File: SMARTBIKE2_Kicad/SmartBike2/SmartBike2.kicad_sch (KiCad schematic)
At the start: 0 parts

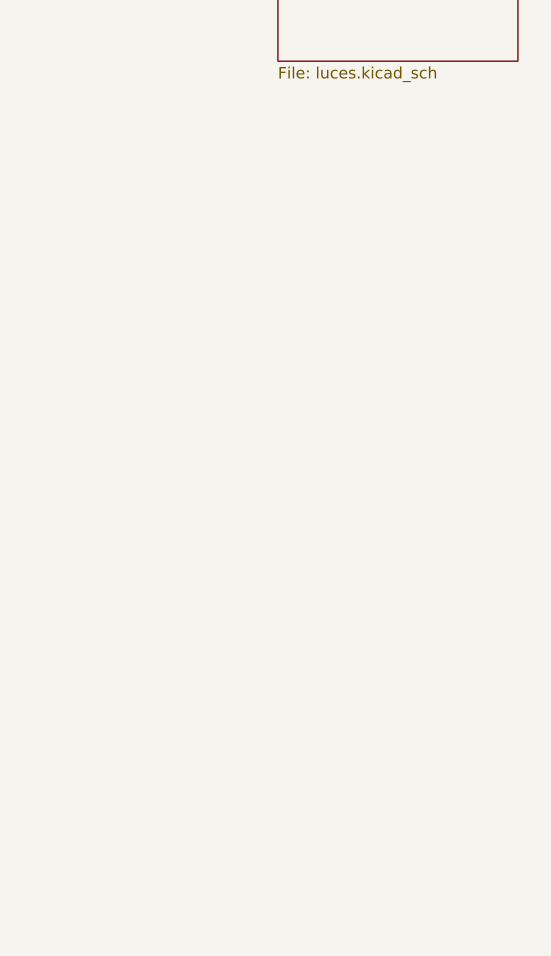
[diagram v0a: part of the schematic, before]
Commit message: Alarma, luces frontales y modulos
+ Circuito luces frontales
+ Conector Luces
+ Conector GPS
+ Conector SIM
+ Conector acelerómetro

~ Acondicionamiento ESP32
~ Huellas
~ PCB
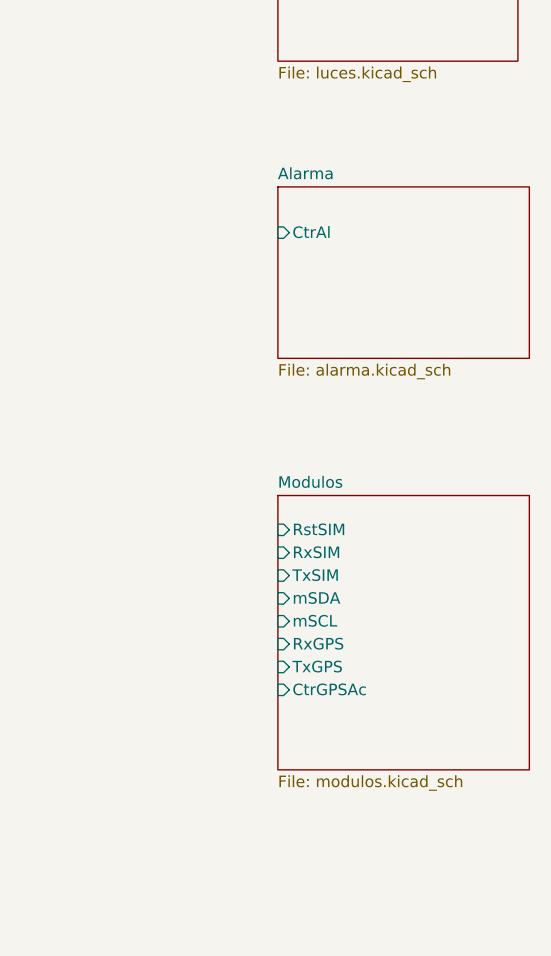
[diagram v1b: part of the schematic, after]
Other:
- added sheet Alarma (alarma.kicad_sch)
- added sheet Modulos (modulos.kicad_sch)
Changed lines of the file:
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@@
 (kicad_sch (version 20230121) (generator eeschema)
   (paper "A4")
+  (sheet (at 232.41 71.12) (size 27.94 19.05) (fields_autoplaced)
+    (stroke (width 0.1524) (type solid))
+    (fill (color 0 0 0 0.0000))
+    (property "Sheetname" "Alarma" (at 232.41 70.4084 0)
+      (effects (font (size 1.27 1.27)) (justify left bottom))
+    )
+    (property "Sheetfile" "alarma.kicad_sch" (at 232.41 90.7546 0)
+      (effects (font (size 1.27 1.27)) (justify left top))
+    )
+    (pin "CtrAl" input (at 232.41 76.2 180)
+      (effects (font (size 1.27 1.27)) (justify left))
+    )
+    (instances
+      (project "SmartBike2"
+        (path "/ec60d9f0-678c-40dc-aaf4-e99b29a92238" (page "6"))
+      )
+    )
+  )
   (sheet (at 232.41 35.56) (size 26.67 21.59) (fields_autoplaced)
     (stroke (width 0.1524) (type solid))
@@
       )
     )
+  )
+  (sheet (at 232.41 105.41) (size 27.94 30.48) (fields_autoplaced)
+    (stroke (width 0.1524) (type solid))
+    (fill (color 0 0 0 0.0000))
+    (property "Sheetname" "Modulos" (at 232.41 104.6984 0)
+      (effects (font (size 1.27 1.27)) (justify left bottom))
+    )
+    (property "Sheetfile" "modulos.kicad_sch" (at 232.41 136.4746 0)
+      (effects (font (size 1.27 1.27)) (justify left top))
+    )
+    (pin "RstSIM" input (at 232.41 109.22 180)
+      (effects (font (size 1.27 1.27)) (justify left))
+    )
+    (pin "RxSIM" input (at 232.41 111.76 180)
+      (effects (font (size 1.27 1.27)) (justify left))
+    )
+    (pin "TxSIM" input (at 232.41 114.3 180)
+      (effects (font (size 1.27 1.27)) (justify left))
+    )
+    (pin "mSDA" input (at 232.41 116.84 180)
+      (effects (font (size 1.27 1.27)) (justify left))
+    )
+    (pin "mSCL" input (at 232.41 119.38 180)
+      (effects (font (size 1.27 1.27)) (justify left))
+    )
+    (pin "RxGPS" input (at 232.41 121.92 180)
+      (effects (font (size 1.27 1.27)) (justify left))
+    )
+    (pin "TxGPS" input (at 232.41 124.46 180)
+      (effects (font (size 1.27 1.27)) (justify left))
+    )
+    (pin "CtrGPSAc" input (at 232.41 127 180)
+      (effects (font (size 1.27 1.27)) (justify left))
+    )
+    (instances
+      (project "SmartBike2"
+        (path "/ec60d9f0-678c-40dc-aaf4-e99b29a92238" (page "7"))
+      )
+    )

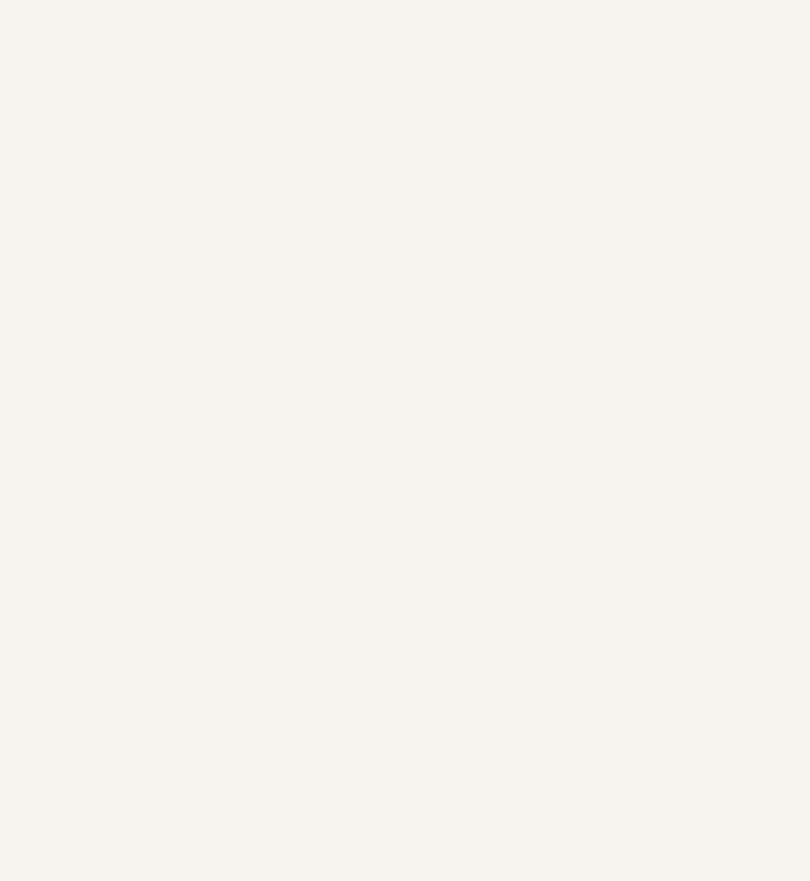
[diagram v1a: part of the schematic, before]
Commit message: Simbolo ESP32
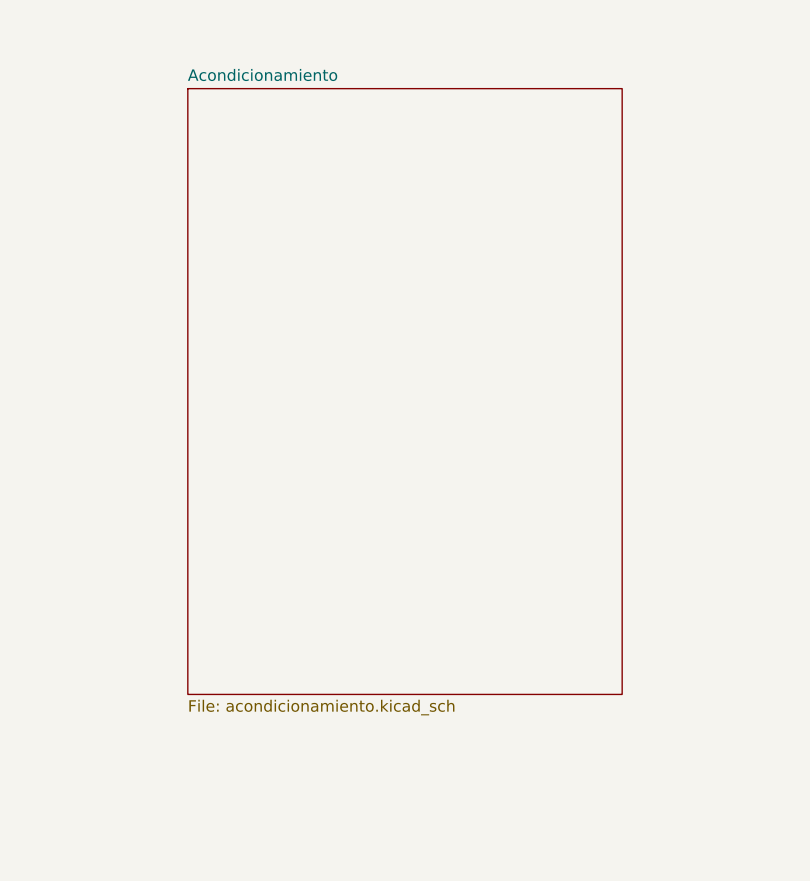
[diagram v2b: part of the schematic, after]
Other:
- added sheet Acondicionamiento (acondicionamiento.kicad_sch)
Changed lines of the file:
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@@
+    )
+  )
+  (sheet (at 58.42 40.64) (size 48.26 67.31) (fields_autoplaced)
+    (stroke (width 0.1524) (type solid))
+    (fill (color 0 0 0 0.0000))
+    (property "Sheetname" "Acondicionamiento" (at 58.42 39.9284 0)
+      (effects (font (size 1.27 1.27)) (justify left bottom))
+    )
+    (property "Sheetfile" "acondicionamiento.kicad_sch" (at 58.42 108.5346 0)
+      (effects (font (size 1.27 1.27)) (justify left top))
+    )
+    (instances
+      (project "SmartBike2"
+        (path "/ec60d9f0-678c-40dc-aaf4-e99b29a92238" (page "8"))
+      )
     )
   )

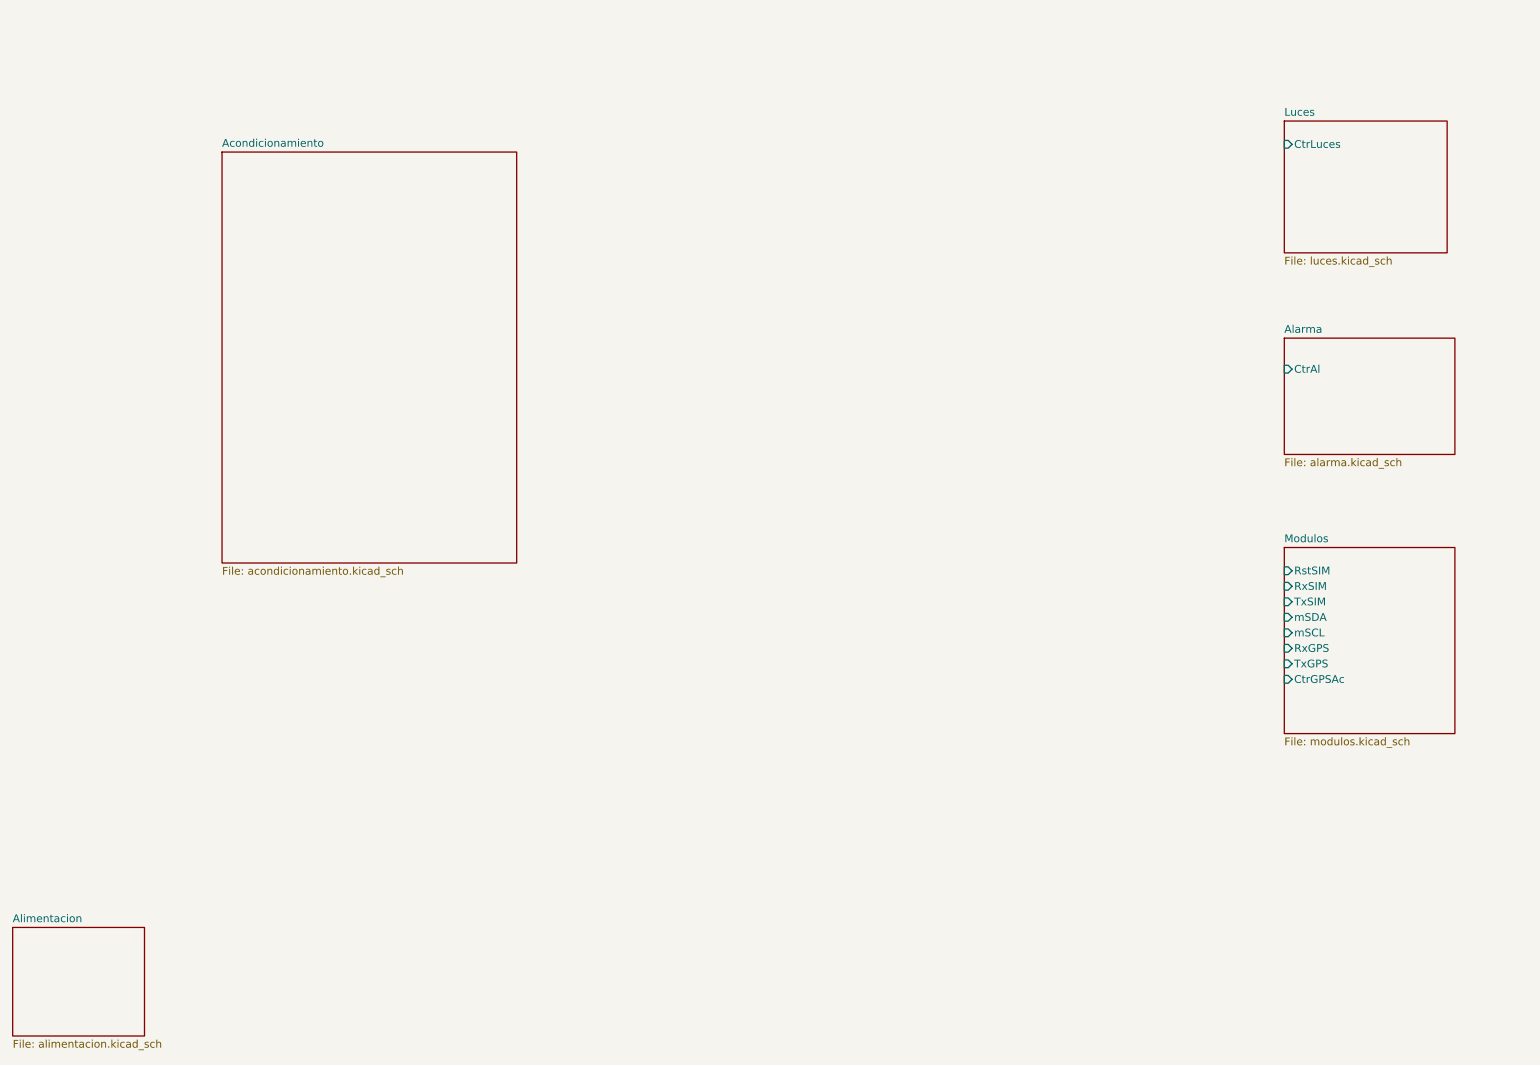
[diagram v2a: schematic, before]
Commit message: Beta 100% esquemáticos
+ Acondicionamiento ESP32

~ Huellas
~ PCB
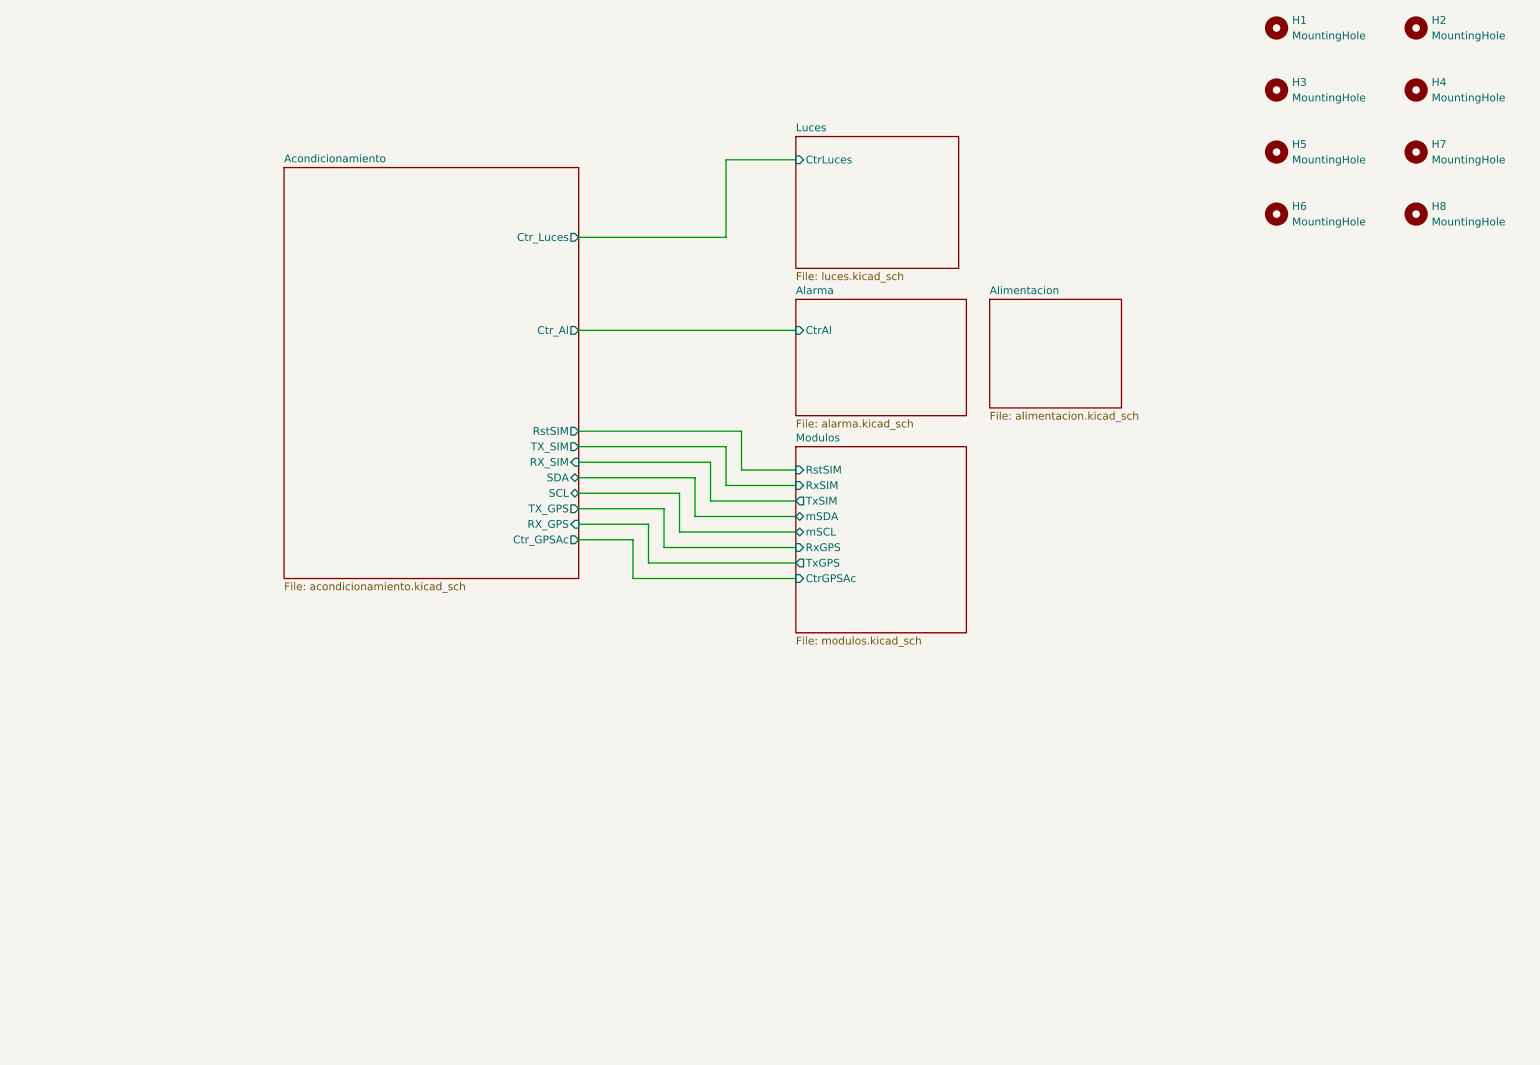
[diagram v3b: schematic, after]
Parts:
- added H1, H2, H3, H4, H5, H6, H7, H8: MountingHole, symbol Mechanical:MountingHole
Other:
- sheet Acondicionamiento ports: added Ctr_Al, Ctr_GPSAc, Ctr_Luces, RX_GPS, RX_SIM, RstSIM, SCL, SDA, TX_GPS, TX_SIM; removed none

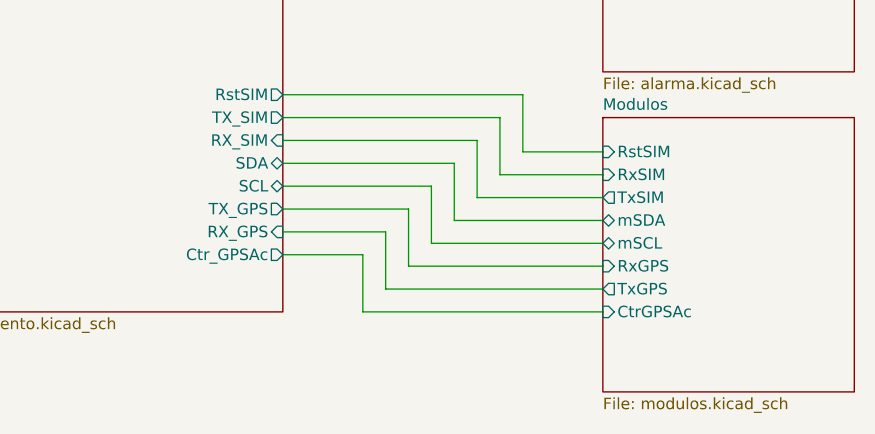
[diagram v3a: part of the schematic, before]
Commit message: cambio alimentacion GPS
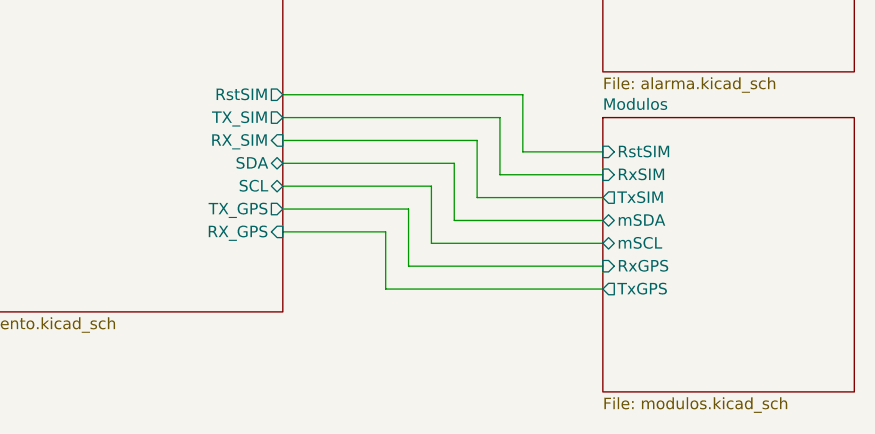
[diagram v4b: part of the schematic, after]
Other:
- sheet Acondicionamiento ports: added none; removed Ctr_GPSAc
- sheet Modulos ports: added none; removed CtrGPSAc
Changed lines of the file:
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@@
 (kicad_sch (version 20230121) (generator eeschema)
   (paper "A4")
-  (wire (pts (xy 116.84 104.14) (xy 125.73 104.14))
-    (stroke (width 0) (type default))
-  )
   (wire (pts (xy 116.84 54.61) (xy 140.97 54.61))
     (stroke (width 0) (type default))
@@
     (stroke (width 0) (type default))
   )
-  (wire (pts (xy 125.73 110.49) (xy 152.4 110.49))
-    (stroke (width 0) (type default))
-  )
   (wire (pts (xy 130.81 99.06) (xy 116.84 99.06))
     (stroke (width 0) (type default))
@@
     (stroke (width 0) (type default))
   )
-  (wire (pts (xy 125.73 104.14) (xy 125.73 110.49))
-    (stroke (width 0) (type default))
-  )
   (wire (pts (xy 152.4 105.41) (xy 130.81 105.41))
     (stroke (width 0) (type default))
@@
       (effects (font (size 1.27 1.27)) (justify left))
     )
-    (pin "CtrGPSAc" input (at 152.4 110.49 180)
-      (effects (font (size 1.27 1.27)) (justify left))
-    )
     (instances
       (project "SmartBike2"
@@
       (effects (font (size 1.27 1.27)) (justify right))
     )
-    (pin "Ctr_GPSAc" output (at 116.84 104.14 0)
-      (effects (font (size 1.27 1.27)) (justify right))
-    )

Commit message: mas huellas
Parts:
- H1, H2, H3, H4, H5, H6, H7, H8: footprint (none) -> MountingHole:MountingHole_3.2mm_M3
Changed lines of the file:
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@@
       (effects (font (size 1.27 1.27)) (justify left))
     )
-    (property "Footprint" "" (at 231.14 20.32 0)
+    (property "Footprint" "MountingHole:MountingHole_3.2mm_M3" (at 231.14 20.32 0)
       (effects (font (size 1.27 1.27)) hide)
     )
@@
       (effects (font (size 1.27 1.27)) (justify left))
     )
-    (property "Footprint" "" (at 231.14 50.8 0)
+    (property "Footprint" "MountingHole:MountingHole_3.2mm_M3" (at 231.14 50.8 0)
       (effects (font (size 1.27 1.27)) hide)
     )
@@
       (effects (font (size 1.27 1.27)) (justify left))
     )
-    (property "Footprint" "" (at 254 20.32 0)
+    (property "Footprint" "MountingHole:MountingHole_3.2mm_M3" (at 254 20.32 0)
       (effects (font (size 1.27 1.27)) hide)
     )
@@
       (effects (font (size 1.27 1.27)) (justify left))
     )
-    (property "Footprint" "" (at 254 50.8 0)
+    (property "Footprint" "MountingHole:MountingHole_3.2mm_M3" (at 254 50.8 0)
       (effects (font (size 1.27 1.27)) hide)
     )
@@
       (effects (font (size 1.27 1.27)) (justify left))
     )
-    (property "Footprint" "" (at 231.14 30.48 0)
+    (property "Footprint" "MountingHole:MountingHole_3.2mm_M3" (at 231.14 30.48 0)
       (effects (font (size 1.27 1.27)) hide)
     )
@@
       (effects (font (size 1.27 1.27)) (justify left))
     )
-    (property "Footprint" "" (at 254 40.64 0)
+    (property "Footprint" "MountingHole:MountingHole_3.2mm_M3" (at 254 40.64 0)
       (effects (font (size 1.27 1.27)) hide)
     )
@@
       (effects (font (size 1.27 1.27)) (justify left))
     )
-    (property "Footprint" "" (at 231.14 40.64 0)
+    (property "Footprint" "MountingHole:MountingHole_3.2mm_M3" (at 231.14 40.64 0)
       (effects (font (size 1.27 1.27)) hide)
     )
@@
       (effects (font (size 1.27 1.27)) (justify left))
     )
-    (property "Footprint" "" (at 254 30.48 0)
+    (property "Footprint" "MountingHole:MountingHole_3.2mm_M3" (at 254 30.48 0)
       (effects (font (size 1.27 1.27)) hide)
     )
